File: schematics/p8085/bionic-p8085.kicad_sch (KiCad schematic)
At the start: 5 parts, among them J1 Bionic-P135, J2 Bionic-P245, U1 P8085AH, U3 11AA010-I/TO

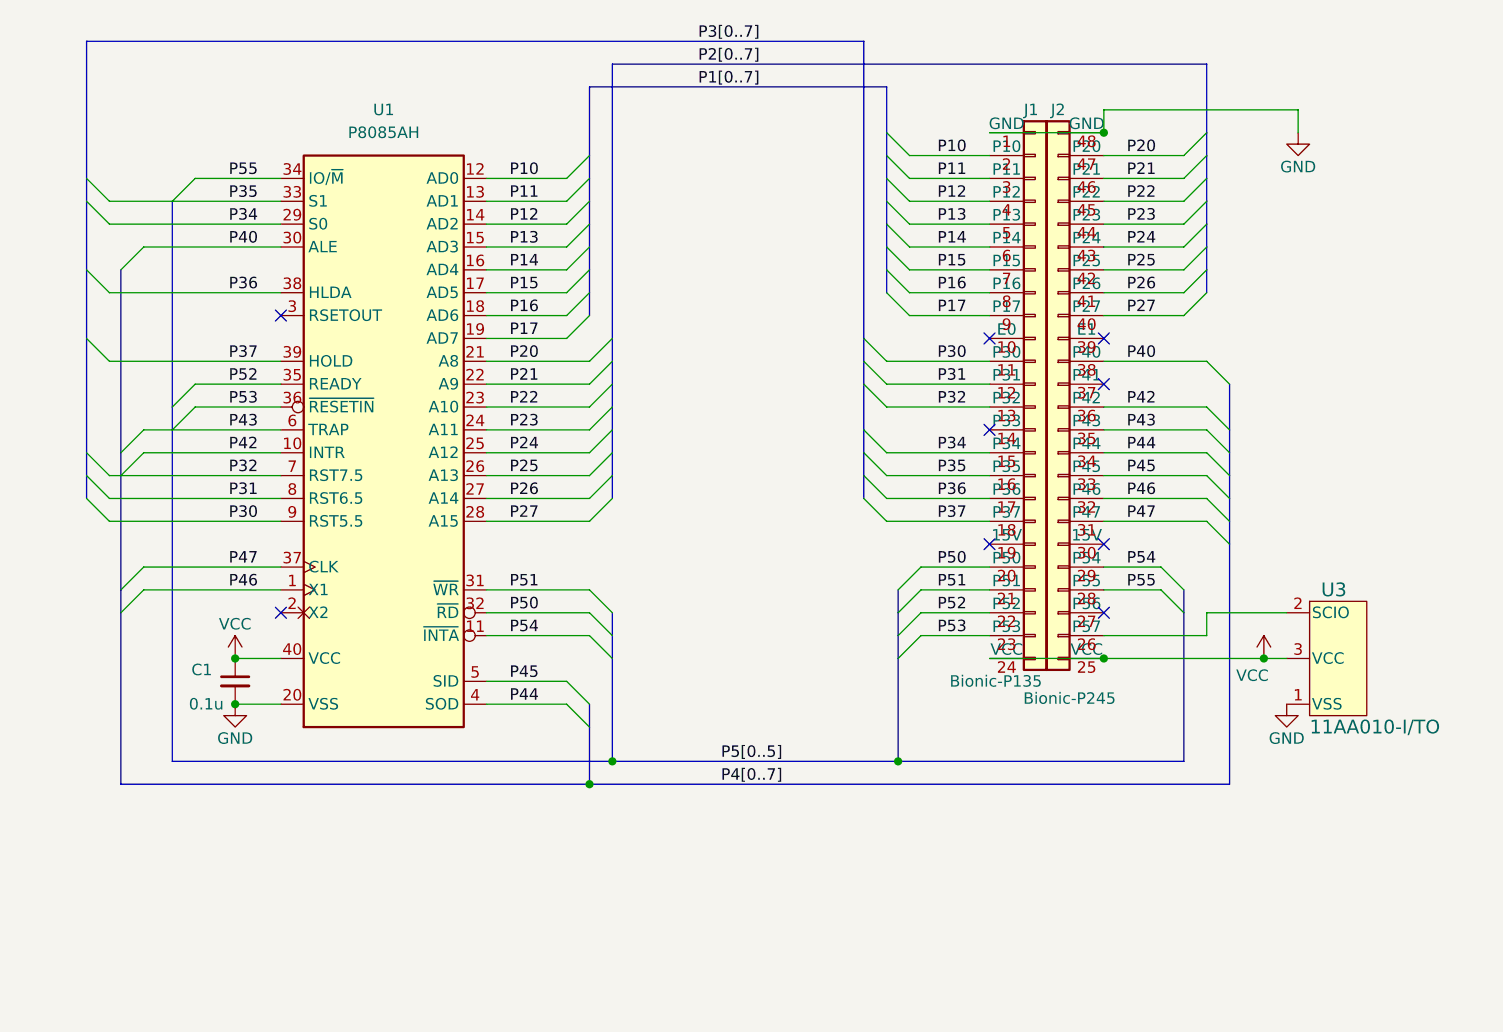
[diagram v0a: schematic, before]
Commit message: [P8085] Read control signals as bus
Assign control signals, S0, S1, #RD, #WR and #INTA to P9 and read
those signals at once.
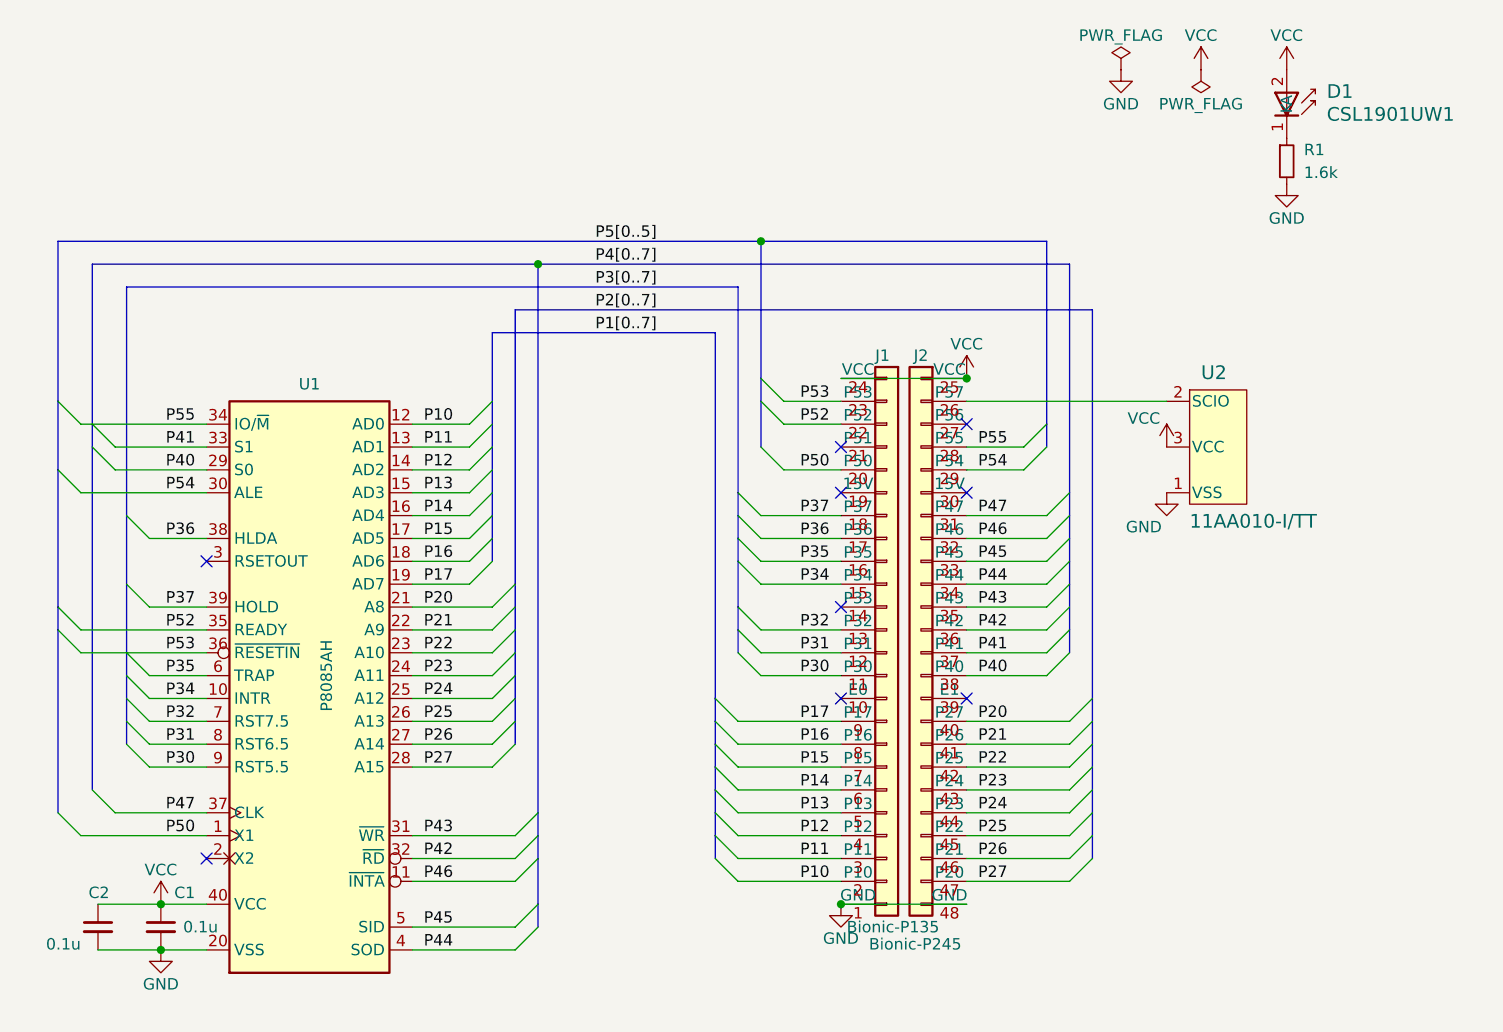
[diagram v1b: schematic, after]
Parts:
- removed U3: 11AA010-I/TO, TO-92_MC_MCH, symbol 0-LocalLibrary:11AA010-I_TO
- added C2: 0.1u, Capacitor_SMD:C_0603_1608Metric_Pad1.08x0.95mm_HandSolder, symbol Device:C_Small
- added D1: CSL1901UW1, 0-LocalLibrary:LED_CSL1901UW1_ROM, symbol 0-LocalLibrary:CSL1901UW1
- added R1: 1.6k, Resistor_SMD:R_0603_1608Metric_Pad0.98x0.95mm_HandSolder, symbol Device:R_Small
- added U2: 11AA010-I/TT, 0-LocalLibrary:SOT-23_MC_MCH-M, symbol 0-LocalLibrary:11AA010-I_TT
- C1: footprint Capacitor_THT:C_Disc_D3.4mm_W2.1mm_P2.50mm -> Capacitor_SMD:C_0603_1608Metric_Pad1.08x0.95mm_HandSolder
- J1: footprint connector:Bionic-P135_Vertical -> 0-LocalLibrary:Bionic-P135_Vertical
- J2: footprint connector:Bionic-P245_Vertical -> 0-LocalLibrary:Bionic-P245_Vertical
- U1: footprint Package_DIP:DIP-40_W15.24mm -> 0-LocalLibrary:DIP-40_W15.24mm_Socket
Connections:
- net GND: now also C2.2, R1.2, U2.1 (VSS)
- net P20: now also J2.40 (P27); no longer J2.47 (P20)
- net P21: now also J2.41 (P26); no longer J2.46 (P21)
- net P22: now also J2.42 (P25); no longer J2.45 (P22)
- net P23: now also J2.43 (P24); no longer J2.44 (P23)
- net P24: now also J2.44 (P23); no longer J2.43 (P24)
- net P25: now also J2.45 (P22); no longer J2.42 (P25)
- net P26: now also J2.46 (P21); no longer J2.41 (P26)
- net P27: now also J2.47 (P20); no longer J2.40 (P27)
- net P34: now also U1.10 (INTR); no longer U1.29 (S0)
- net P35: now also U1.6 (TRAP); no longer U1.33 (S1)
- net P40: now also U1.29 (S0); no longer U1.30 (ALE)
- net P42: now also U1.32 (~{RD}); no longer U1.10 (INTR)
- net P43: now also U1.31 (~{WR}); no longer U1.6 (TRAP)
- net P46: now also U1.11 (~{INTA}); no longer U1.1 (X1)
- net P50: now also U1.1 (X1); no longer U1.32 (~{RD})
- net P54: now also U1.30 (ALE); no longer U1.11 (~{INTA})
- net VCC: now also C2.1, D1.2 (A), U2.3 (VCC)
- net at J2.26 (P57): now also U2.2 (SCIO)
- net P41: now reaches J2.37 (P41)
- net P41: now also U1.33 (S1)
- net P51: no longer names the net of J1.21 (P51)
- net P51: no longer U1.31 (~{WR})
- new net: D1.1 (K), R1.1
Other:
- moved on the sheet: C1, U1

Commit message: [P8085] Connect RESET OUT pin
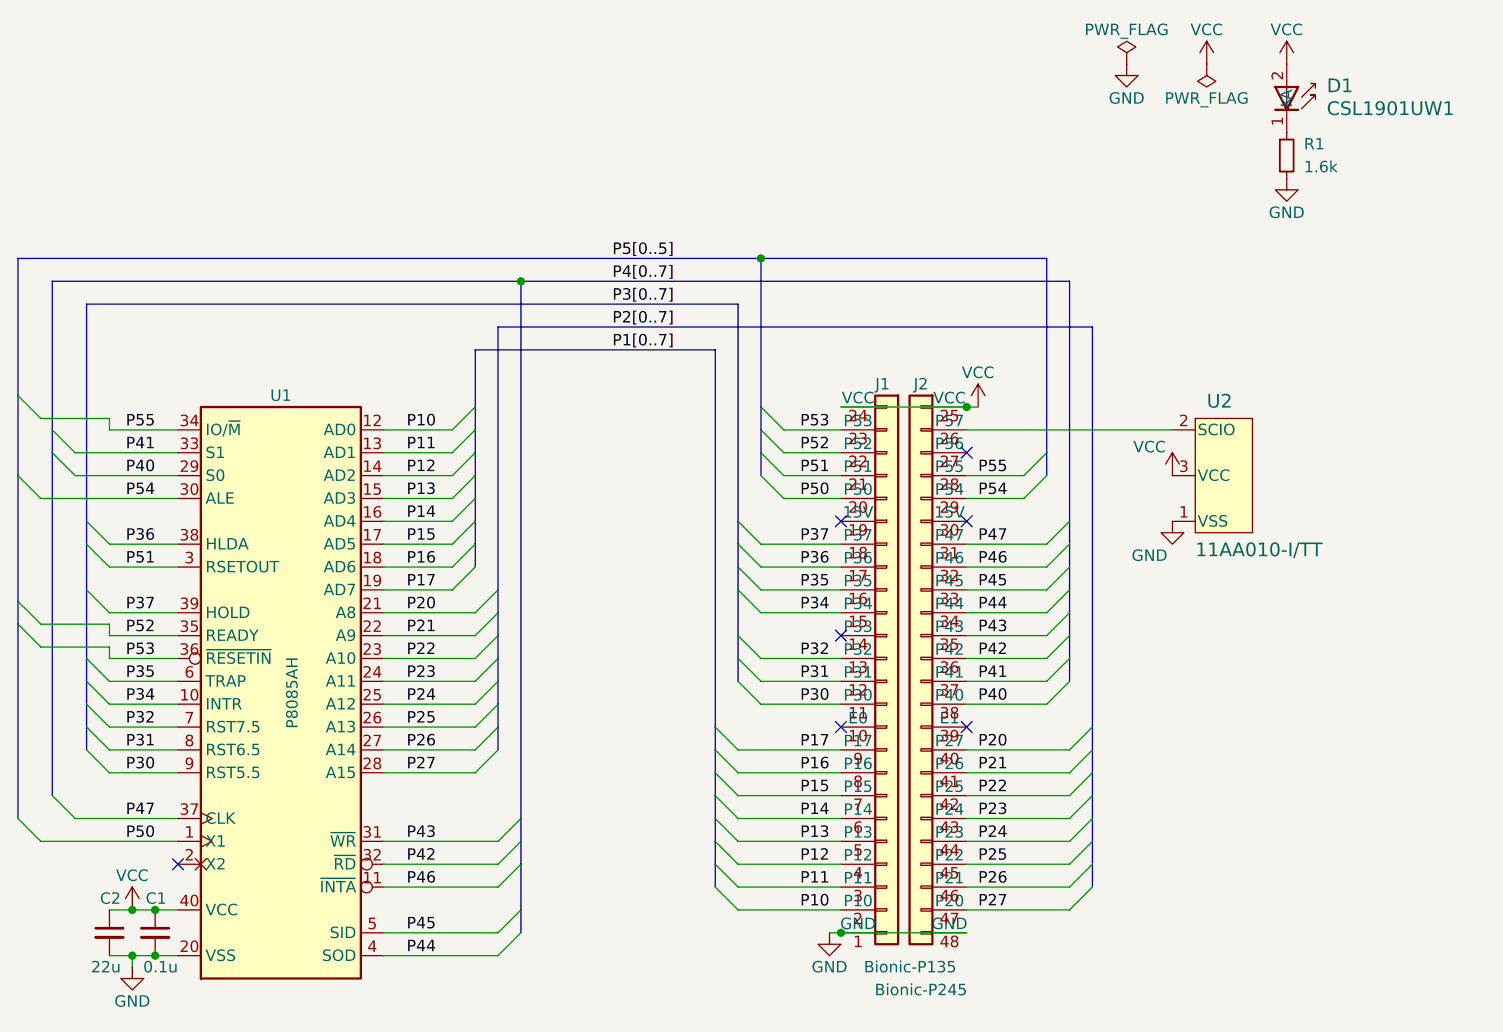
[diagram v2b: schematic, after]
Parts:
- C2: value 0.1u -> 22u
- J1: footprint 0-LocalLibrary:Bionic-P135_Vertical -> connector:Bionic-P135_Vertical
- J2: footprint 0-LocalLibrary:Bionic-P245_Vertical -> connector:Bionic-P245_Vertical
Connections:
- net P51: now reaches J1.21 (P51)
- net P51: now also U1.3 (RSETOUT)
- no-connect marks 9 -> 7
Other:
- moved on the sheet: C1, C2, D1, R1, U2

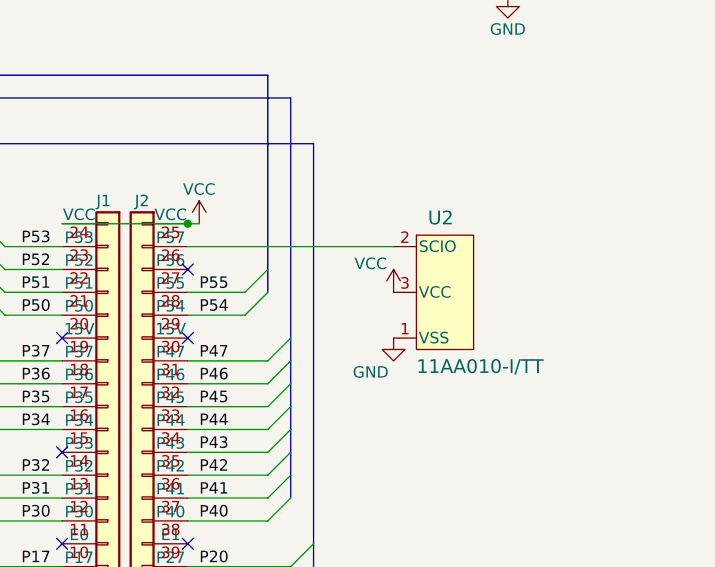
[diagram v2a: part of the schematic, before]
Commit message: [P8085] Fix EEPROM pinout
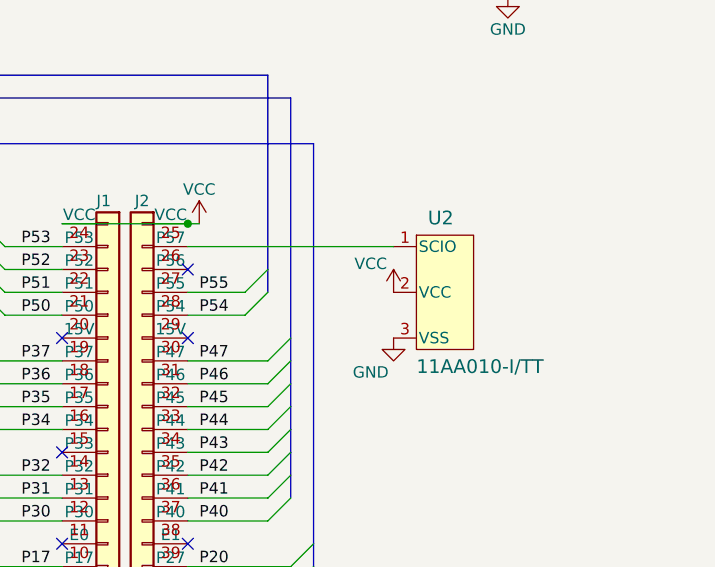
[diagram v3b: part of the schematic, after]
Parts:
- J1: footprint connector:Bionic-P135_Vertical -> 0-LocalLibrary:Bionic-P135_Vertical
- J2: footprint connector:Bionic-P245_Vertical -> 0-LocalLibrary:Bionic-P245_Vertical
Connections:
- net GND: now also U2.3 (VSS); no longer U2.1 (VSS)
- net VCC: now also U2.2 (VCC); no longer U2.3 (VCC)
- net at J2.26 (P57): now also U2.1 (SCIO); no longer U2.2 (SCIO)
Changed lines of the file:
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@@
   (title_block
     (title "BionicP8085")
-    (date "2024-10-25")
-    (rev "5")
+    (date "2024-11-01")
+    (rev "6")
     (company "Tadashi G. Takaoka")
   )
@@
       (effects (font (size 1.27 1.27)))
     )
-    (property "Footprint" "connector:Bionic-P245_Vertical" (at 172.72 139.7 0)
+    (property "Footprint" "0-LocalLibrary:Bionic-P245_Vertical" (at 172.72 139.7 0)
       (effects (font (size 1.27 1.27)) hide)
     )
@@
       (effects (font (size 1.27 1.27)) (justify left))
     )
-    (property "Footprint" "connector:Bionic-P135_Vertical" (at 165.1 139.7 0)
-      (effects (font (size 1.27 1.27)) hide)
-    )
+    (property "Footprint" "0-LocalLibrary:Bionic-P135_Vertical" (at 165.1 139.7 0)
+      (effects (font (size 1.27 1.27)) hide)
+    )

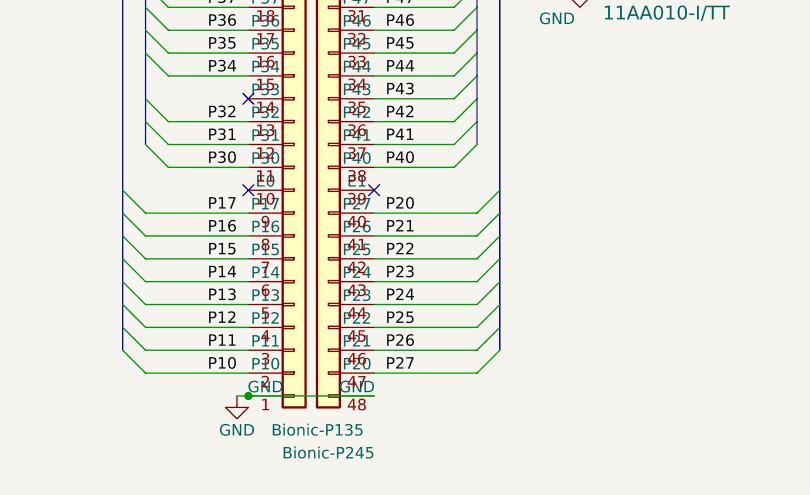
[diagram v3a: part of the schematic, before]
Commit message: [P8085] Shrink board size
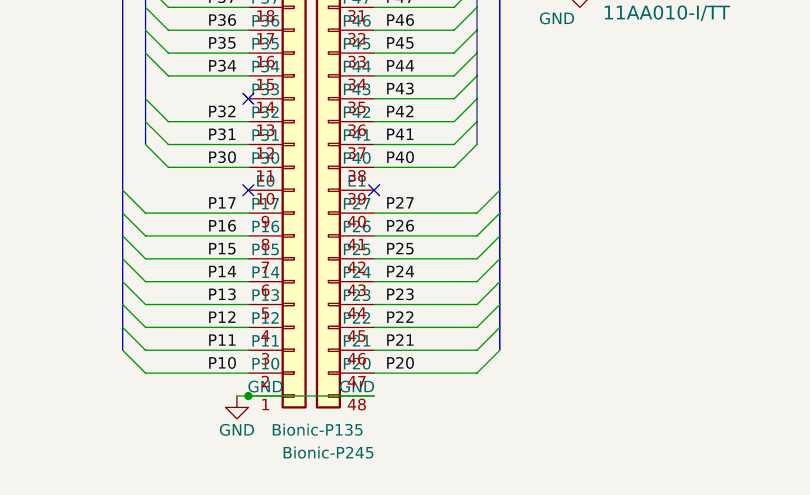
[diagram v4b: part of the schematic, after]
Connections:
- net P20: now also J2.47 (P20); no longer J2.40 (P27)
- net P21: now also J2.46 (P21); no longer J2.41 (P26)
- net P22: now also J2.45 (P22); no longer J2.42 (P25)
- net P23: now also J2.44 (P23); no longer J2.43 (P24)
- net P24: now also J2.43 (P24); no longer J2.44 (P23)
- net P25: now also J2.42 (P25); no longer J2.45 (P22)
- net P26: now also J2.41 (P26); no longer J2.46 (P21)
- net P27: now also J2.40 (P27); no longer J2.47 (P20)
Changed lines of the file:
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@@
   (title_block
     (title "BionicP8085")
-    (date "2024-11-01")
+    (date "2024-12-02")
     (rev "6")
     (company "Tadashi G. Takaoka")
@@
     (effects (font (size 1.27 1.27)) (justify right bottom))
   )
-  (label "P24" (at 173.99 124.46 0) (fields_autoplaced)
+  (label "P24" (at 173.99 121.92 0) (fields_autoplaced)
     (effects (font (size 1.27 1.27)) (justify left bottom))
   )
@@
     (effects (font (size 1.27 1.27)) (justify left bottom))
   )
-  (label "P26" (at 173.99 129.54 0) (fields_autoplaced)
+  (label "P26" (at 173.99 116.84 0) (fields_autoplaced)
     (effects (font (size 1.27 1.27)) (justify left bottom))
   )
@@
     (effects (font (size 1.27 1.27)) (justify left bottom))
   )
-  (label "P25" (at 173.99 127 0) (fields_autoplaced)
+  (label "P25" (at 173.99 119.38 0) (fields_autoplaced)
     (effects (font (size 1.27 1.27)) (justify left bottom))
   )
@@
     (effects (font (size 1.27 1.27)) (justify right bottom))
   )
-  (label "P22" (at 173.99 119.38 0) (fields_autoplaced)
+  (label "P22" (at 173.99 127 0) (fields_autoplaced)
     (effects (font (size 1.27 1.27)) (justify left bottom))
   )
@@
     (effects (font (size 1.27 1.27)) (justify right bottom))
   )
-  (label "P21" (at 173.99 116.84 0) (fields_autoplaced)
+  (label "P21" (at 173.99 129.54 0) (fields_autoplaced)
     (effects (font (size 1.27 1.27)) (justify left bottom))
   )
@@
     (effects (font (size 1.27 1.27)) (justify left bottom))
   )
-  (label "P23" (at 173.99 121.92 0) (fields_autoplaced)
+  (label "P23" (at 173.99 124.46 0) (fields_autoplaced)
     (effects (font (size 1.27 1.27)) (justify left bottom))
   )
@@
     (effects (font (size 1.27 1.27)) (justify left bottom))
   )
-  (label "P27" (at 173.99 132.08 0) (fields_autoplaced)
+  (label "P27" (at 173.99 114.3 0) (fields_autoplaced)
     (effects (font (size 1.27 1.27)) (justify left bottom))
   )
@@
     (effects (font (size 1.27 1.27)) (justify right bottom))
   )
-  (label "P20" (at 173.99 114.3 0) (fields_autoplaced)
-    (effects (font (size 1.27 1.27)) (justify left bottom))
-  )
+  (label "P20" (at 173.99 132.08 0) (fields_autoplaced)
+    (effects (font (size 1.27 1.27)) (justify left bottom))
+  )

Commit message: [schematics] Update LED footprint
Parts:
- D1: footprint 0-LocalLibrary:LED_CSL1901UW1_ROM -> 0-LocalLibrary:LED_CSL1901UW1_ROM-M
